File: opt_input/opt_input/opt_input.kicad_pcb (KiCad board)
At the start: 2 copper layers, 18.1 x 12.1 mm, 4 parts, among them J1 Conn_01x03, U1 TSOP34S40F

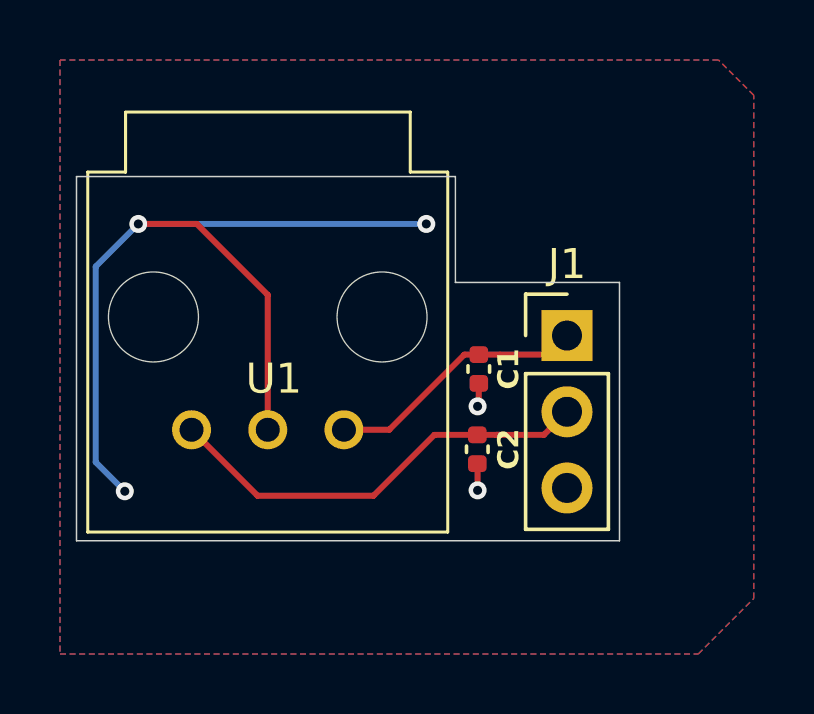
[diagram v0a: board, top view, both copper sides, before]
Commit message: Adjusting outline optical reciever, fixing silkscreen errors
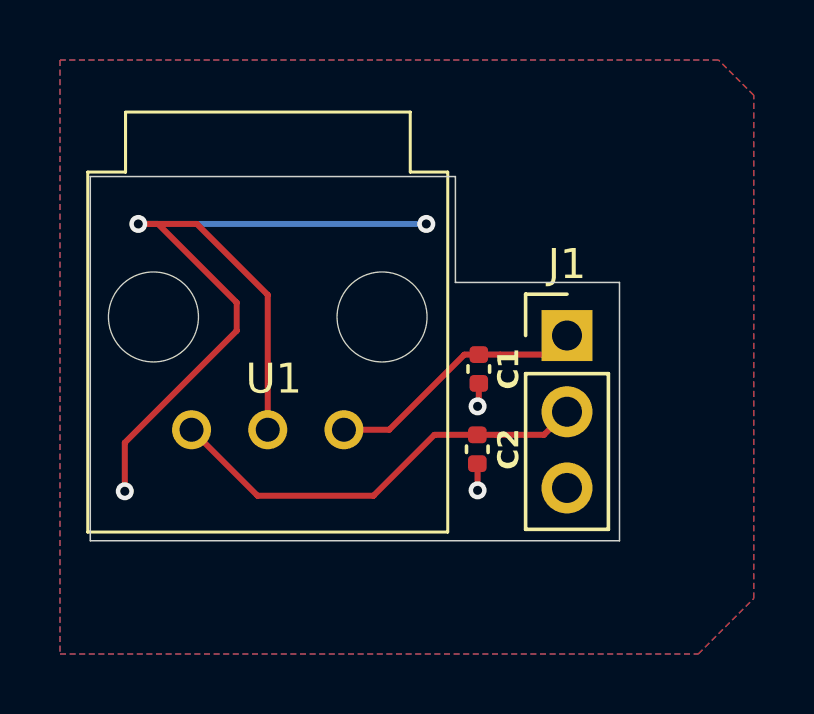
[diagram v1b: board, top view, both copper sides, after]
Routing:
- net GND: track 31.0 -> 33.3 mm
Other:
- board size 18.1 x 12.1 mm -> 17.6 x 12.1 mm
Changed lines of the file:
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@@
 		)
 		(embedded_fonts no)
-		(model "${KICAD10_3DMODEL_DIR}/Connector_PinHeader_2.54mm.3dshapes/PinHeader_1x03_P2.54mm_Vertical.step"
-			(offset
-				(xyz 0 0 0)
-			)
-			(scale
-				(xyz 1 1 1)
-			)
-			(rotate
-				(xyz 0 0 0)
-			)
-		)
 	)
 	(footprint "components:FCR684218R"
@@
 	)
 	(gr_line
-		(start 139.55 72.91)
-		(end 139.55 85.05)
+		(start 140.01 72.91)
+		(end 140.01 85.05)
 		(stroke
 			(width 0.05)
@@
 	)
 	(gr_line
-		(start 139.55 85.05)
+		(start 140.01 85.05)
 		(end 157.65 85.05)
 		(stroke
@@
 	(gr_line
 		(start 152.18 72.91)
-		(end 139.55 72.91)
+		(end 140.01 72.91)
 		(stroke
 			(width 0.05)
@@
 	)
 	(segment
+		(start 141.16 83.4)
+		(end 141.16 81.78)
+		(width 0.2)
+		(layer "F.Cu")
+		(net "GND")
+	)
+	(segment
 		(start 152.92 82.49)
 		(end 152.91 82.48)
@@
 	)
 	(segment
+		(start 141.16 81.78)
+		(end 144.89 78.05)
+		(width 0.2)
+		(layer "F.Cu")
+		(net "GND")
+	)
+	(segment
 		(start 145.925 81.35)
 		(end 145.925 76.855)
@@
 	)
 	(segment
+		(start 142.27 74.49)
+		(end 141.61 74.49)
+		(width 0.2)
+		(layer "F.Cu")
+		(net "GND")
+	)
+	(segment
 		(start 145.925 76.855)
 		(end 143.56 74.49)
@@
 	)
 	(segment
+		(start 144.89 78.05)
+		(end 144.89 77.11)
+		(width 0.2)
+		(layer "F.Cu")
+		(net "GND")
+	)
+	(segment
 		(start 152.92 83.37)
 		(end 152.92 82.49)
+		(width 0.2)
+		(layer "F.Cu")
+		(net "GND")
+	)
+	(segment
+		(start 144.89 77.11)
+		(end 142.27 74.49)
 		(width 0.2)
 		(layer "F.Cu")
@@
 	)
 	(segment
-		(start 141.61 74.49)
-		(end 140.19 75.91)
-		(width 0.2)
-		(layer "B.Cu")
-		(net "GND")
-	)
-	(segment
-		(start 140.19 75.91)
-		(end 140.19 82.43)
-		(width 0.2)
-		(layer "B.Cu")
-		(net "GND")
-	)
-	(segment
 		(start 151.21 74.49)
 		(end 141.61 74.49)
 		(width 0.2)
 		(layer "B.Cu")
-		(net "GND")
-	)
-	(segment
-		(start 140.19 82.43)
-		(end 141.16 83.4)
-		(width 0.2)
-		(layer "B.Cu")
